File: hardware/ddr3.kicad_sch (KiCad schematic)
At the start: 23 parts, among them U2 H5TQ4G63EFR

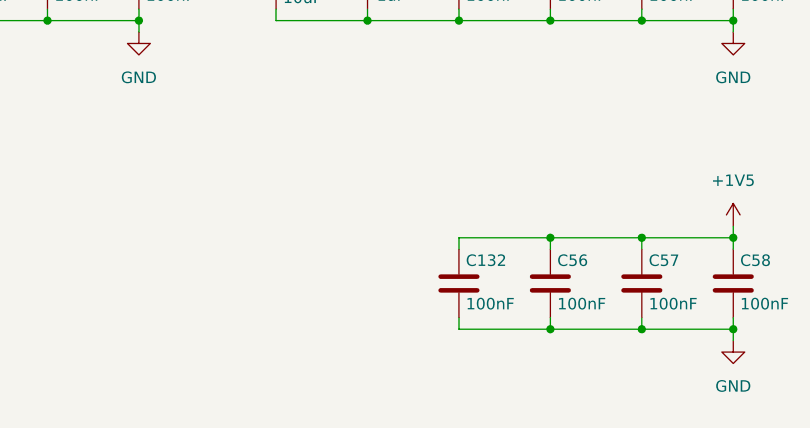
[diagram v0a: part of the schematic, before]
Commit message: Add some more decoupling and move trace
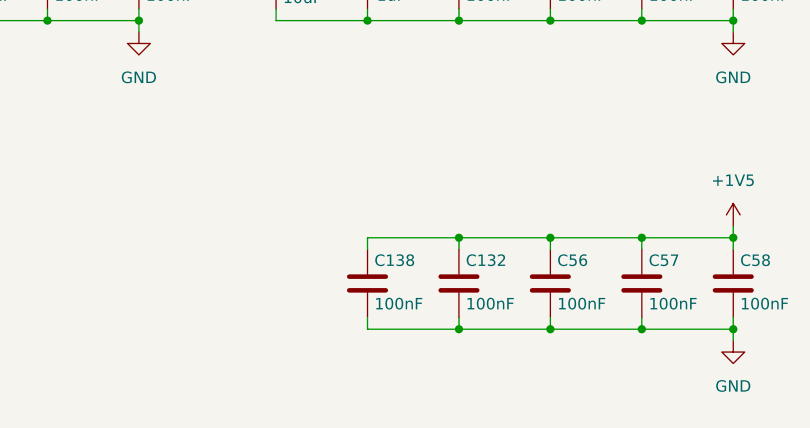
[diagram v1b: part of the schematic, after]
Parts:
- added C138: 100nF, Capacitor_SMD:C_0402_1005Metric, symbol Device:C
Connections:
- net +1V5: now also C138.1
- net GND: now also C138.2
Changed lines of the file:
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@@
 	)
 	(junction
+		(at 233.68 142.24)
+		(diameter 0)
+		(color 0 0 0 0)
+	)
+	(junction
 		(at 187.96 107.95)
 		(diameter 0)
@@
 	)
 	(junction
+		(at 233.68 152.4)
+		(diameter 0)
+		(color 0 0 0 0)
+	)
+	(junction
 		(at 264.16 107.95)
 		(diameter 0)
@@
 		)
 	)
+	(wire
+		(pts
+			(xy 223.52 152.4) (xy 223.52 151.13)
+		)
+		(stroke
+			(width 0)
+			(type default)
+		)
+	)
 	(bus
 		(pts
@@
 	(wire
 		(pts
+			(xy 223.52 142.24) (xy 233.68 142.24)
+		)
+		(stroke
+			(width 0)
+			(type default)
+		)
+	)
+	(wire
+		(pts
 			(xy 68.58 147.32) (xy 77.47 147.32)
 		)
@@
 	(wire
 		(pts
+			(xy 223.52 143.51) (xy 223.52 142.24)
+		)
+		(stroke
+			(width 0)
+			(type default)
+		)
+	)
+	(wire
+		(pts
 			(xy 162.56 81.28) (xy 162.56 80.01)
 		)
@@
 		)
 	)
+	(wire
+		(pts
+			(xy 233.68 152.4) (xy 223.52 152.4)
+		)
+		(stroke
+			(width 0)
+			(type default)
+		)
+	)
 	(bus
 		(pts
@@
 					(unit 1)
 				)
+			)
+		)
+	)
+	(symbol
+		(lib_id "Device:C")
+		(at 223.52 147.32 0)
+		(unit 1)
+		(exclude_from_sim no)
+		(in_bom yes)
+		(on_board yes)
+		(dnp no)
+		(property "Reference" "C138"
+			(at 224.282 144.78 0)
+			(effects
+				(font
+					(size 1.27 1.27)
+				)
+				(justify left)
+			)
+		)
+		(property "Value" "100nF"
+			(at 224.282 149.606 0)
+			(effects
+				(font
+					(size 1.27 1.27)
+				)
+				(justify left)
+			)
+		)
+		(property "Footprint" "Capacitor_SMD:C_0402_1005Metric"
+			(at 224.4852 151.13 0)
+			(effects
+				(font
+					(size 1.27 1.27)
+				)
+				(hide yes)
+			)
+		)
+		(property "Datasheet" "~"
+			(at 223.52 147.32 0)
+			(effects
+				(font
+					(size 1.27 1.27)
+				)
+				(hide yes)
+			)
+		)
+		(property "Description" "Unpolarized capacitor"
+			(at 223.52 147.32 0)
+			(effects
+				(font
+					(size 1.27 1.27)
+				)
+				(hide yes)
+			)
+		)
+		(property "LCSC Part #" "C1525"
+			(at 223.52 147.32 0)
+			(effects
+				(font
+					(size 1.27 1.27)
+				)
+				(hide yes)
+			)
+		)
+		(property "FT Position Offset" ""
+			(at 223.52 147.32 0)
+			(effects
+				(font
+					(size 1.27 1.27)
+				)
+				(hide yes)
+			)
+		)
+		(property "FT Rotation Offset" ""
+			(at 223.52 147.32 0)
+			(effects
+				(font
+					(size 1.27 1.27)
+				)
+				(hide yes)
+			)
+		)
+		(pin "2"
+		)
+		(pin "1"
+		)
+		(instances
+			(project "cm0"
+				(path "/b53f5dbb-8078-4818-9e8f-fdf90ba6d854/32a4bb18-2695-4537-bbd4-f872ec13cb53"
+					(reference "C138")
+					(unit 1)
+				)
